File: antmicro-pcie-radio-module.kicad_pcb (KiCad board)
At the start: 4 copper layers, 80.2 x 22.2 mm, 48 parts, among them J1 U_FL-R-SMT_10_, U1 UPD720202, U2 SST25VF512A, U3 CoralAccelerator, U4 NRF52840, Y1 NX3225SA-24M

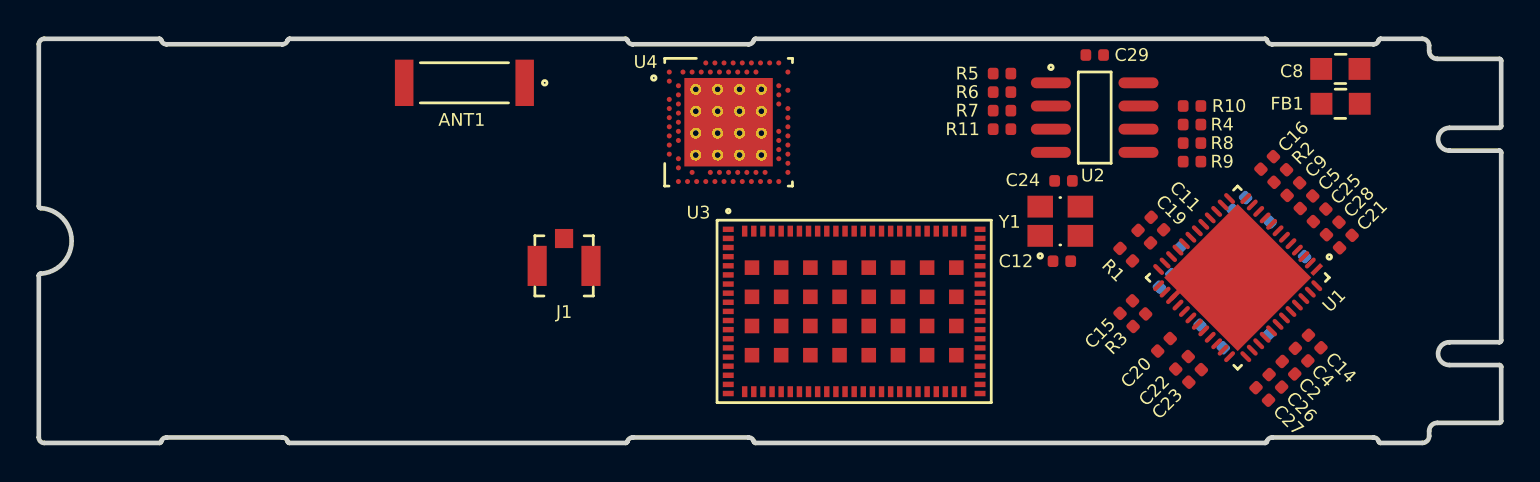
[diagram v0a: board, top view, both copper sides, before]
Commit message: Add M.2 B+M edge connector
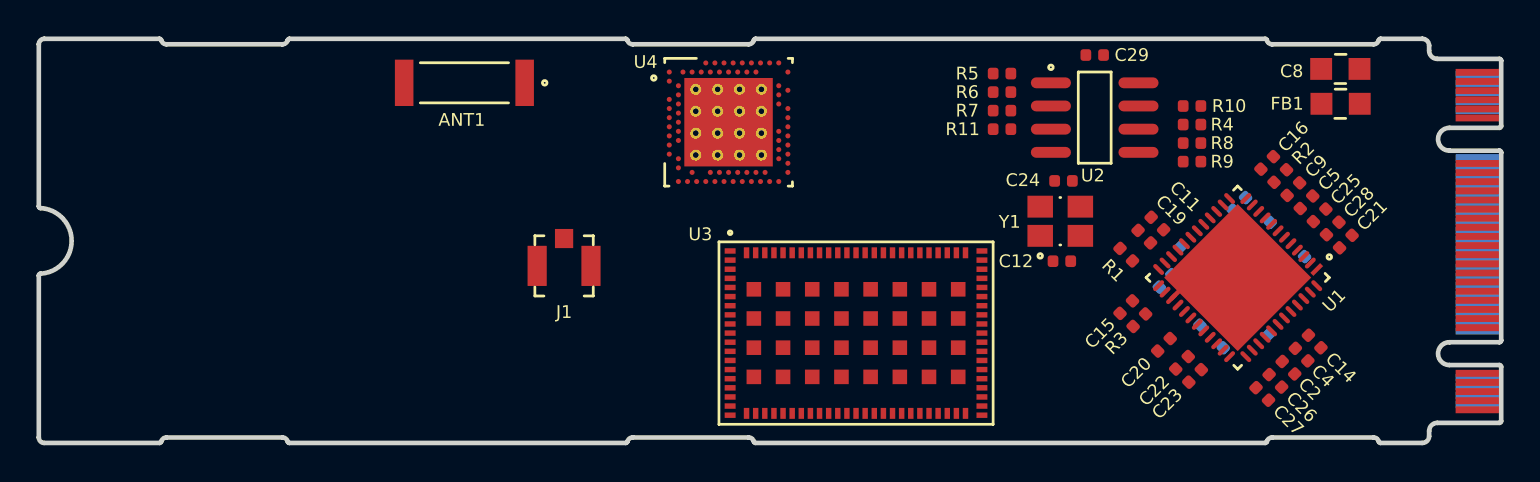
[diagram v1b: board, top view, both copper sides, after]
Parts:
- added J2: M.2-M+B-Pins, pcie-radio-module:M.2 M+B Keys, F.Cu at (194.9, 97.0)
- moved U3 1.19 mm to (159.5, 107.6)

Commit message: Initial work on RF part
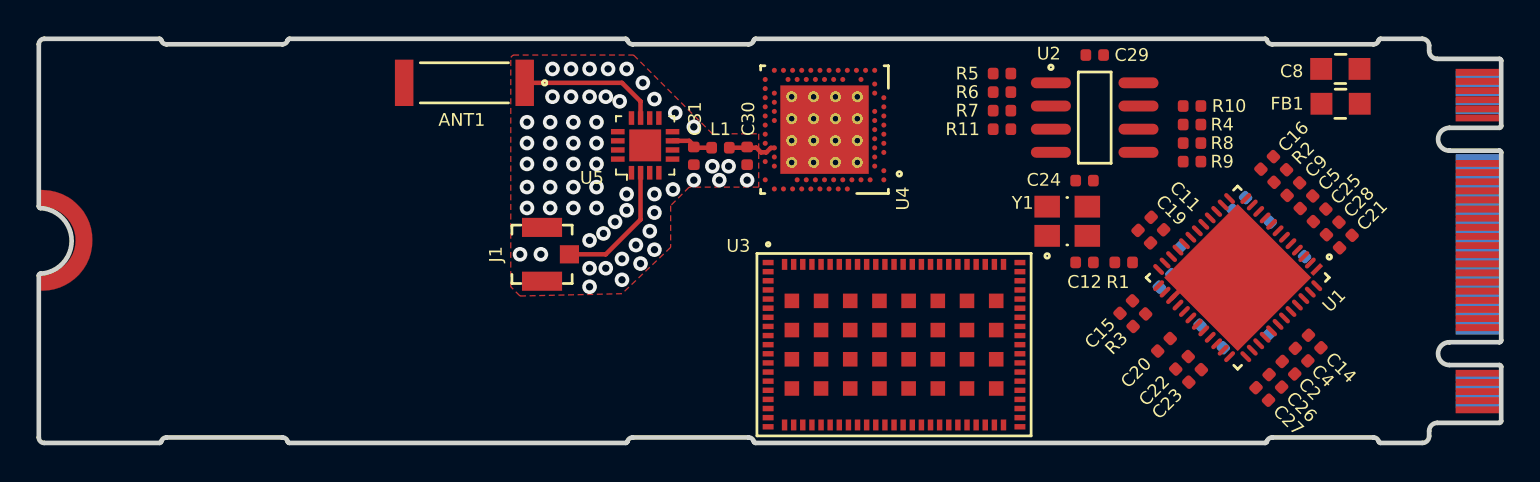
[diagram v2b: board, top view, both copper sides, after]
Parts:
- added C30: RF_Capacitor, pcie-radio-module:0402-cap, F.Cu at (153.5, 97.9)
- added C31: RF_Capacitor, pcie-radio-module:0402-cap, F.Cu at (150.6, 97.9)
- added L1: RF_Inductor, pcie-radio-module:0402-res, F.Cu at (152.1, 97.4)
- added REF**: M.2 Stud, pcie-radio-module:M.2 Stud, F.Cu at (115.3, 102.4)
- added U5: PE42423MLBA-Z, pcie-radio-module:VFQFN-16-1EP_3x3mm, F.Cu at (148.0, 97.3)
- moved U4 5.27 mm to (157.8, 96.4), turned to 180 degrees
- moved U3 2.18 mm to (161.6, 108.2)
- moved J1 1.36 mm to (142.3, 103.3), turned to 90 degrees
- moved C12 1.24 mm to (172.0, 103.7)
- moved C24 1.15 mm to (172.0, 99.2)
- moved R1 0.45 mm to (174.2, 103.7), turned to 0 degrees
- moved Y1 0.38 mm to (171.1, 101.4)
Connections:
- J1 pad 1: Net-(J1-Pad1) -> GND
- J2 pad 41: Net-(J2-Pad41) -> PERX_N
- J2 pad 43: Net-(J2-Pad43) -> PERX_P
- J2 pad 47: Net-(J2-Pad47) -> PETX_N
- J2 pad 49: Net-(J2-Pad49) -> PETX_P
- J2 pad 50: Net-(J2-Pad50) -> ~PERST
- J2 pad 52: Net-(J2-Pad52) -> ~PECREQ
- J2 pad 53: Net-(J2-Pad53) -> PECLK_N
- J2 pad 54: Net-(J2-Pad54) -> ~PEWAKE
- J2 pad 55: Net-(J2-Pad55) -> PECLK_P
- U4 pad E24: Net-(U4-PadE24) -> Net-(U4-PadB5)
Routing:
- net Net-(ANT1-Pad1): track 0.00 -> 7.66 mm
- net Net-(J1-Pad2): track 0.00 -> 7.10 mm
- net Net-(C30-Pad1): track 0.00 -> 2.65 mm
- net Net-(C31-Pad1): track 0.00 -> 2.30 mm
- net GND: vias 0 -> 58
- added copper zone on F.Cu, net GND
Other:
- net class Default: clearance 0.2 -> 0.127
- rule trace_clearance: 0.2 -> 0.127
